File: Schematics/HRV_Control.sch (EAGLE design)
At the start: 32 parts, among them IC1 5v

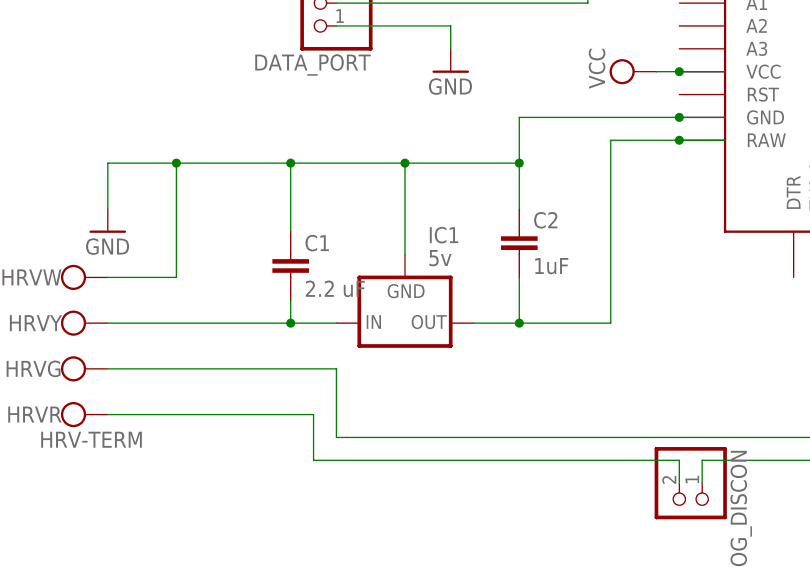
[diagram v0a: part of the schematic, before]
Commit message: Misc. enhancements
- Revised algorithms for fresh air and dehumidification for improved
efficiency.
- Added ClearEeprom function initiatated by sending code 5 from to
microprocessor.
- Revised circuit board to fix errors with voltage regulator pinout and
resistor sizes.
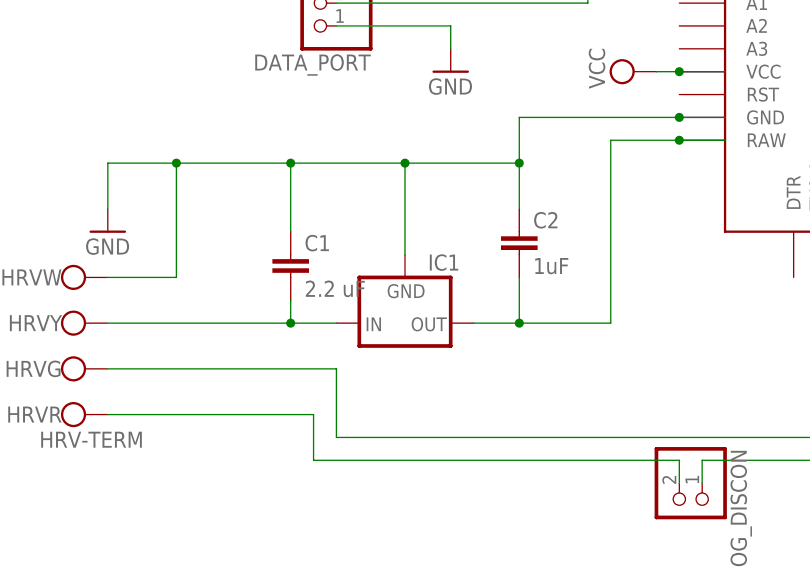
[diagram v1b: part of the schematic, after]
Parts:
- C1: device resistor:C-EU025-024X044 -> capacitor-wima:C5/3
- IC1: value 5v -> (none); device v-reg:79XXS -> v-reg:78XXL
- R1, R2, R3, R4, R5, R6, R7: device resistor:R-EU_0204/5 -> resistor:R-EU_0204/7
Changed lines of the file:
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@@
 </classes>
 <parts>
-<part name="IC1" library="v-reg" deviceset="79XXS" device="" value="5v"/>
 <part name="GND1" library="supply1" deviceset="GND" device=""/>
-<part name="C1" library="resistor" deviceset="C-EU" device="025-024X044" value="2.2 uF"/>
+<part name="C1" library="capacitor-wima" deviceset="C" device="5/3" value="2.2 uF"/>
 <part name="C2" library="resistor" deviceset="C-EU" device="025-024X044" value="1uF"/>
 <part name="SUPPLY1" library="supply2" deviceset="VCC" device=""/>
@@
 <part name="GND3" library="supply1" deviceset="GND" device=""/>
 <part name="GND4" library="supply1" deviceset="GND" device=""/>
-<part name="R1" library="resistor" deviceset="R-EU_" device="0204/5" value="10K"/>
-<part name="R2" library="resistor" deviceset="R-EU_" device="0204/5" value="10K"/>
-<part name="R3" library="resistor" deviceset="R-EU_" device="0204/5" value="10K"/>
+<part name="R1" library="resistor" deviceset="R-EU_" device="0204/7" value="10K"/>
+<part name="R2" library="resistor" deviceset="R-EU_" device="0204/7" value="10K"/>
+<part name="R3" library="resistor" deviceset="R-EU_" device="0204/7" value="10K"/>
 <part name="HRV" library="HRV_Control" deviceset="HRV-TERM" device=""/>
 <part name="GND5" library="supply1" deviceset="GND" device=""/>
 <part name="SUPPLY5" library="supply2" deviceset="VCC" device=""/>
-<part name="R4" library="resistor" deviceset="R-EU_" device="0204/5" value="1K"/>
-<part name="R5" library="resistor" deviceset="R-EU_" device="0204/5" value="2.2K"/>
+<part name="R4" library="resistor" deviceset="R-EU_" device="0204/7" value="1K"/>
+<part name="R5" library="resistor" deviceset="R-EU_" device="0204/7" value="2.2K"/>
 <part name="GND6" library="supply1" deviceset="GND" device=""/>
 <part name="FAN-OUT" library="solpad" deviceset="SE14" device=""/>
@@
 <part name="SUPPLY6" library="supply2" deviceset="VCC" device=""/>
 <part name="GND8" library="supply1" deviceset="GND" device=""/>
-<part name="R6" library="resistor" deviceset="R-EU_" device="0204/5" value="10K"/>
+<part name="R6" library="resistor" deviceset="R-EU_" device="0204/7" value="10K"/>
 <part name="SUPPLY7" library="supply2" deviceset="VCC" device=""/>
 <part name="GND9" library="supply1" deviceset="GND" device=""/>
-<part name="R7" library="resistor" deviceset="R-EU_" device="0204/5" value="10K"/>
+<part name="R7" library="resistor" deviceset="R-EU_" device="0204/7" value="10K"/>
 <part name="CLOCK-MODULE" library="HRV_Control" deviceset="DS1307RTC" device=""/>
 <part name="GND10" library="supply1" deviceset="GND" device=""/>
@@
 <part name="HC-06" library="con-lsta" deviceset="FE04-1" device=""/>
 <part name="GND15" library="supply1" deviceset="GND" device=""/>
+<part name="IC1" library="v-reg" deviceset="78XXL" device=""/>
 </parts>
 <sheets>
@@
 </plain>
 <instances>
-<instance part="IC1" gate="1" x="43.18" y="17.78"/>
 <instance part="GND1" gate="1" x="10.16" y="27.94"/>
 <instance part="C1" gate="G$1" x="30.48" y="25.4"/>
@@
 <instance part="HC-06" gate="G$1" x="45.72" y="99.06" rot="R270"/>
 <instance part="GND15" gate="1" x="-22.86" y="147.32"/>
+<instance part="IC1" gate="A" x="43.18" y="17.78" rot="MR180"/>
 </instances>
 <busses>
@@
 <wire x1="73.66" y1="38.1" x2="66.04" y2="38.1" width="0.1524" layer="91"/>
 <wire x1="66.04" y1="38.1" x2="66.04" y2="17.78" width="0.1524" layer="91"/>
-<pinref part="IC1" gate="1" pin="OUT"/>
 <wire x1="66.04" y1="17.78" x2="55.88" y2="17.78" width="0.1524" layer="91"/>
 <pinref part="C2" gate="G$1" pin="2"/>
-<wire x1="55.88" y1="17.78" x2="50.8" y2="17.78" width="0.1524" layer="91"/>
 <wire x1="55.88" y1="22.86" x2="55.88" y2="17.78" width="0.1524" layer="91"/>
-<junction x="55.88" y="17.78"/>
 <pinref part="U$6" gate="G$1" pin="RAW"/>
 <junction x="73.66" y="38.1"/>
+<pinref part="IC1" gate="A" pin="OUT"/>
+<wire x1="50.8" y1="17.78" x2="55.88" y2="17.78" width="0.1524" layer="91"/>
+<junction x="55.88" y="17.78"/>
 </segment>
 </net>
 <net name="N$1" class="0">
 <segment>
-<pinref part="IC1" gate="1" pin="IN"/>
 <wire x1="10.16" y1="17.78" x2="30.48" y2="17.78" width="0.1524" layer="91"/>
 <pinref part="C1" gate="G$1" pin="2"/>
-<wire x1="30.48" y1="17.78" x2="35.56" y2="17.78" width="0.1524" layer="91"/>
 <wire x1="30.48" y1="20.32" x2="30.48" y2="17.78" width="0.1524" layer="91"/>
 <pinref part="HRV" gate="Y" pin="KL"/>
+<pinref part="IC1" gate="A" pin="IN"/>
+<wire x1="35.56" y1="17.78" x2="30.48" y2="17.78" width="0.1524" layer="91"/>
 <junction x="30.48" y="17.78"/>
 </segment>
@@
 <pinref part="C1" gate="G$1" pin="1"/>
 <wire x1="30.48" y1="35.56" x2="30.48" y2="27.94" width="0.1524" layer="91"/>
-<pinref part="IC1" gate="1" pin="GND"/>
 <wire x1="43.18" y1="25.4" x2="43.18" y2="35.56" width="0.1524" layer="91"/>
 <wire x1="30.48" y1="35.56" x2="43.18" y2="35.56" width="0.1524" layer="91"/>
@@
 <pinref part="U$6" gate="G$1" pin="GND"/>
 <junction x="73.66" y="40.64"/>
-</segment>
-<segment>
+<pinref part="IC1" gate="A" pin="GND"/>
+</segment>
+<segment>
